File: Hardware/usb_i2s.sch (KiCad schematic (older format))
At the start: 13 parts, among them J2 USB_B, U8 USBLC6-2SC6, U9 PCM2707, Y1 12 MHz

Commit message: started routing
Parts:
- Y1: symbol Device:Crystal -> Device:Crystal_GND24
- renumbered C2 to C76, C7 to C77, C9 to C78, J2 to J8, R11 to R39, R13 to R40, R18 to R41, R19 to R42, R20 to R43, R37 to R44
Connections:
- wire segments 85 -> 91
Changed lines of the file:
@@
 $Descr A4 11693 8268
 encoding utf-8
-Sheet 7 7
+Sheet 6 8
 Title ""
 Date ""
@@
 $EndComp
 $Comp
-L Device:Crystal Y?
+L Device:Crystal_GND24 Y?
 U 1 1 61ACFD71
 P 2200 4950
@@
 AR Path="/5AFACF29/61ACFD77" Ref="C?"  Part="1"
 AR Path="/61ACFD77" Ref="C?"  Part="1"
-AR Path="/61AABE2E/61ACFD77" Ref="C7"  Part="1"
-F 0 "C7" H 2565 5196 50  0000 L CNN
+AR Path="/61AABE2E/61ACFD77" Ref="C77"  Part="1"
+F 0 "C77" H 2565 5196 50  0000 L CNN
 F 1 "33p" H 2565 5105 50  0000 L CNN
 F 2 "Capacitor_SMD:C_0603_1608Metric_Pad1.08x0.95mm_HandSolder" H 2488 5000 50  0001 C CNN
@@
 $EndComp
 $Comp
-L dsp-amplifier-x4-rescue:GND #PWR?
+L power:GND #PWR?
 U 1 1 61ACFD7D
 P 3550 6050
 AR Path="/61ACFD7D" Ref="#PWR?"  Part="1"
-AR Path="/61AABE2E/61ACFD7D" Ref="#PWR0129"  Part="1"
-F 0 "#PWR0129" H 3550 5800 50  0001 C CNN
+AR Path="/61AABE2E/61ACFD7D" Ref="#PWR0107"  Part="1"
+F 0 "#PWR0107" H 3550 5800 50  0001 C CNN
 F 1 "GND" H 3550 5900 50  0000 C CNN
 F 2 "" H 3550 6050 50  0001 C CNN
@@
 AR Path="/5AFACF29/61ACFD91" Ref="C?"  Part="1"
 AR Path="/61ACFD91" Ref="C?"  Part="1"
-AR Path="/61AABE2E/61ACFD91" Ref="C2"  Part="1"
-F 0 "C2" H 2065 5196 50  0000 L CNN
+AR Path="/61AABE2E/61ACFD91" Ref="C76"  Part="1"
+F 0 "C76" H 2065 5196 50  0000 L CNN
 F 1 "33p" H 2065 5105 50  0000 L CNN
 F 2 "Capacitor_SMD:C_0603_1608Metric_Pad1.08x0.95mm_HandSolder" H 1988 5000 50  0001 C CNN
@@
 	2450 4950 2450 5000
 $Comp
-L dsp-amplifier-x4-rescue:GND #PWR?
+L power:GND #PWR?
 U 1 1 61ACFD9B
 P 2200 5450
 AR Path="/61ACFD9B" Ref="#PWR?"  Part="1"
-AR Path="/61AABE2E/61ACFD9B" Ref="#PWR0130"  Part="1"
-F 0 "#PWR0130" H 2200 5200 50  0001 C CNN
+AR Path="/61AABE2E/61ACFD9B" Ref="#PWR0104"  Part="1"
+F 0 "#PWR0104" H 2200 5200 50  0001 C CNN
 F 1 "GND" H 2200 5300 50  0000 C CNN
 F 2 "" H 2200 5450 50  0001 C CNN
@@
 P 4150 3200
 AR Path="/61ACFDAE" Ref="#PWR?"  Part="1"
-AR Path="/61AABE2E/61ACFDAE" Ref="#PWR0131"  Part="1"
-F 0 "#PWR0131" H 4150 3050 50  0001 C CNN
+AR Path="/61AABE2E/61ACFDAE" Ref="#PWR0110"  Part="1"
+F 0 "#PWR0110" H 4150 3050 50  0001 C CNN
 F 1 "+3.3V" H 4165 3373 50  0000 C CNN
 F 2 "" H 4150 3200 50  0001 C CNN
@@
 P 3650 3200
 AR Path="/61ACFDC0" Ref="#PWR?"  Part="1"
-AR Path="/61AABE2E/61ACFDC0" Ref="#PWR0132"  Part="1"
-F 0 "#PWR0132" H 3650 3050 50  0001 C CNN
+AR Path="/61AABE2E/61ACFDC0" Ref="#PWR0109"  Part="1"
+F 0 "#PWR0109" H 3650 3050 50  0001 C CNN
 F 1 "VBUS" H 3665 3373 50  0000 C CNN
 F 2 "" H 3650 3200 50  0001 C CNN
@@
 AR Path="/5AFACF29/61ACFDC6" Ref="C?"  Part="1"
 AR Path="/61ACFDC6" Ref="C?"  Part="1"
-AR Path="/61AABE2E/61ACFDC6" Ref="C9"  Part="1"
-F 0 "C9" H 4565 5446 50  0000 L CNN
+AR Path="/61AABE2E/61ACFDC6" Ref="C78"  Part="1"
+F 0 "C78" H 4565 5446 50  0000 L CNN
 F 1 "100n" H 4565 5355 50  0000 L CNN
 F 2 "Capacitor_SMD:C_0603_1608Metric_Pad1.08x0.95mm_HandSolder" H 4488 5250 50  0001 C CNN
@@
 P 3350 3200
 AR Path="/61ACFDD5" Ref="#PWR?"  Part="1"
-AR Path="/61AABE2E/61ACFDD5" Ref="#PWR0142"  Part="1"
-F 0 "#PWR0142" H 3350 3050 50  0001 C CNN
+AR Path="/61AABE2E/61ACFDD5" Ref="#PWR0106"  Part="1"
+F 0 "#PWR0106" H 3350 3050 50  0001 C CNN
 F 1 "+3.3V" H 3365 3373 50  0000 C CNN
 F 2 "" H 3350 3200 50  0001 C CNN
@@
 P 1950 3400
 AR Path="/61ACFDE5" Ref="#PWR?"  Part="1"
-AR Path="/61AABE2E/61ACFDE5" Ref="#PWR0143"  Part="1"
-F 0 "#PWR0143" H 1950 3250 50  0001 C CNN
+AR Path="/61AABE2E/61ACFDE5" Ref="#PWR0101"  Part="1"
+F 0 "#PWR0101" H 1950 3250 50  0001 C CNN
 F 1 "+3.3V" H 1965 3573 50  0000 C CNN
 F 2 "" H 1950 3400 50  0001 C CNN
@@
 $EndComp
 $Comp
-L dsp-amplifier-x4-rescue:GND #PWR?
+L power:GND #PWR?
 U 1 1 61ACFDEB
 P 1950 3650
 AR Path="/61ACFDEB" Ref="#PWR?"  Part="1"
-AR Path="/61AABE2E/61ACFDEB" Ref="#PWR0144"  Part="1"
-F 0 "#PWR0144" H 1950 3400 50  0001 C CNN
+AR Path="/61AABE2E/61ACFDEB" Ref="#PWR0102"  Part="1"
+F 0 "#PWR0102" H 1950 3400 50  0001 C CNN
 F 1 "GND" H 1950 3500 50  0000 C CNN
 F 2 "" H 1950 3650 50  0001 C CNN
@@
 PSEL
 $Comp
-L dsp-amplifier-x4-rescue:GND #PWR?
+L power:GND #PWR?
 U 1 1 61ACFDF8
 P 1950 4050
 AR Path="/61ACFDF8" Ref="#PWR?"  Part="1"
-AR Path="/61AABE2E/61ACFDF8" Ref="#PWR0145"  Part="1"
-F 0 "#PWR0145" H 1950 3800 50  0001 C CNN
+AR Path="/61AABE2E/61ACFDF8" Ref="#PWR0103"  Part="1"
+F 0 "#PWR0103" H 1950 3800 50  0001 C CNN
 F 1 "GND" H 1950 3900 50  0000 C CNN
 F 2 "" H 1950 4050 50  0001 C CNN
@@
 P 4550 3850
 AR Path="/61ACFE10" Ref="R?"  Part="1"
-AR Path="/61AABE2E/61ACFE10" Ref="R18"  Part="1"
-F 0 "R18" V 4343 3850 50  0000 C CNN
+AR Path="/61AABE2E/61ACFE10" Ref="R41"  Part="1"
+F 0 "R41" V 4343 3850 50  0000 C CNN
 F 1 "33" V 4434 3850 50  0000 C CNN
 F 2 "Resistor_SMD:R_0603_1608Metric_Pad0.98x0.95mm_HandSolder" V 4480 3850 50  0001 C CNN
@@
 P 4550 3950
 AR Path="/61ACFE16" Ref="R?"  Part="1"
-AR Path="/61AABE2E/61ACFE16" Ref="R19"  Part="1"
-F 0 "R19" V 4343 3950 50  0001 C CNN
+AR Path="/61AABE2E/61ACFE16" Ref="R42"  Part="1"
+F 0 "R42" V 4343 3950 50  0001 C CNN
 F 1 "33" V 4434 3950 50  0001 C CNN
 F 2 "Resistor_SMD:R_0603_1608Metric_Pad0.98x0.95mm_HandSolder" V 4480 3950 50  0001 C CNN
@@
 P 4550 4050
 AR Path="/61ACFE1C" Ref="R?"  Part="1"
-AR Path="/61AABE2E/61ACFE1C" Ref="R20"  Part="1"
-F 0 "R20" V 4343 4050 50  0001 C CNN
+AR Path="/61AABE2E/61ACFE1C" Ref="R43"  Part="1"
+F 0 "R43" V 4343 4050 50  0001 C CNN
 F 1 "33" V 4434 4050 50  0001 C CNN
 F 2 "Resistor_SMD:R_0603_1608Metric_Pad0.98x0.95mm_HandSolder" V 4480 4050 50  0001 C CNN
@@
 	4400 3850 4350 3850
 $Comp
-L power:VBUS #PWR0163
+L power:VBUS #PWR0100
 U 1 1 61AEB454
 P 1850 1250
-F 0 "#PWR0163" H 1850 1100 50  0001 C CNN
+F 0 "#PWR0100" H 1850 1100 50  0001 C CNN
 F 1 "VBUS" H 1865 1423 50  0000 C CNN
 F 2 "" H 1850 1250 50  0001 C CNN
@@
 	1850 1350 1850 1250
 $Comp
-L dsp-amplifier-x4-rescue:GND #PWR0164
+L power:GND #PWR098
 U 1 1 61AEB45C
 P 1250 2050
-F 0 "#PWR0164" H 1250 1800 50  0001 C CNN
+F 0 "#PWR098" H 1250 1800 50  0001 C CNN
 F 1 "GND" H 1250 1900 50  0000 C CNN
 F 2 "" H 1250 2050 50  0001 C CNN
@@
 	3300 2050 3950 2050
 $Comp
-L power:VBUS #PWR0165
+L power:VBUS #PWR0108
 U 1 1 61AEB470
 P 3650 1500
-F 0 "#PWR0165" H 3650 1350 50  0001 C CNN
+F 0 "#PWR0108" H 3650 1350 50  0001 C CNN
 F 1 "VBUS" H 3665 1673 50  0000 C CNN
 F 2 "" H 3650 1500 50  0001 C CNN
@@
 	3650 1600 3600 1600
 $Comp
-L dsp-amplifier-x4-rescue:GND #PWR0166
+L power:GND #PWR0105
 U 1 1 61AEB478
 P 2750 1700
-F 0 "#PWR0166" H 2750 1450 50  0001 C CNN
+F 0 "#PWR0105" H 2750 1450 50  0001 C CNN
 F 1 "GND" H 2750 1550 50  0000 C CNN
 F 2 "" H 2750 1700 50  0001 C CNN
@@
 Wire Wire Line
 	2750 1600 2750 1700
-Wire Wire Line
-	1650 1550 2600 1550
-Wire Wire Line
-	1650 1650 2600 1650
-Text Label 4350 2050 0    60   ~ 0
+Text Label 4750 1150 2    60   ~ 0
 USB-DM
-Text Label 4350 1150 0    60   ~ 0
+Text Label 4750 2050 2    60   ~ 0
 USB-DP
 $Comp
-L Device:R R11
+L Device:R R39
 U 1 1 61AEB484
 P 4100 1150
-F 0 "R11" V 3893 1150 50  0000 C CNN
+F 0 "R39" V 3893 1150 50  0000 C CNN
 F 1 "33" V 3984 1150 50  0000 C CNN
 F 2 "Resistor_SMD:R_0603_1608Metric_Pad0.98x0.95mm_HandSolder" V 4030 1150 50  0001 C CNN
@@
 $EndComp
 $Comp
-L Device:R R13
+L Device:R R40
 U 1 1 61AEB48A
 P 4100 2050
-F 0 "R13" V 3893 2050 50  0000 C CNN
+F 0 "R40" V 3893 2050 50  0000 C CNN
 F 1 "33" V 3984 2050 50  0000 C CNN
 F 2 "Resistor_SMD:R_0603_1608Metric_Pad0.98x0.95mm_HandSolder" V 4030 2050 50  0001 C CNN
@@
 	4750 1150 4250 1150
 $Comp
-L Connector:USB_B J2
+L Connector:USB_B J8
 U 1 1 61AEB492
 P 1350 1550
-F 0 "J2" H 1407 2017 50  0000 C CNN
+F 0 "J8" H 1407 2017 50  0000 C CNN
 F 1 "USB_B" H 1407 1926 50  0000 C CNN
 F 2 "Connector_USB:USB_B_TE_5787834_Vertical" H 1500 1500 50  0001 C CNN
@@
 P 4550 4350
 AR Path="/61B18C42" Ref="R?"  Part="1"
-AR Path="/61AABE2E/61B18C42" Ref="R37"  Part="1"
-F 0 "R37" V 4343 4350 50  0001 C CNN
+AR Path="/61AABE2E/61B18C42" Ref="R44"  Part="1"
+F 0 "R44" V 4343 4350 50  0001 C CNN
 F 1 "33" V 4434 4350 50  0001 C CNN
 F 2 "Resistor_SMD:R_0603_1608Metric_Pad0.98x0.95mm_HandSolder" V 4480 4350 50  0001 C CNN
@@
 Wire Wire Line
 	4750 4350 4700 4350
+Wire Wire Line
+	2200 5150 2200 5400
+$Comp
+L power:GND #PWR?
+U 1 1 609F2BC8
+P 1750 5450
+AR Path="/609F2BC8" Ref="#PWR?"  Part="1"
+AR Path="/61AABE2E/609F2BC8" Ref="#PWR099"  Part="1"
+F 0 "#PWR099" H 1750 5200 50  0001 C CNN
+F 1 "GND" H 1750 5300 50  0000 C CNN
+F 2 "" H 1750 5450 50  0001 C CNN
+F 3 "" H 1750 5450 50  0001 C CNN
+	1    1750 5450
+	1    0    0    -1
+$EndComp
+Wire Wire Line
+	1750 5450 1750 4550
+Wire Wire Line
+	1750 4550 2200 4550
+Wire Wire Line
+	2200 4550 2200 4750
+Wire Wire Line
+	2500 1650 1650 1650
+Wire Wire Line
+	2500 1550 1650 1550
+Wire Wire Line
+	2600 1550 2500 1650
+Wire Wire Line
+	2500 1550 2600 1650
 $EndSCHEMATC

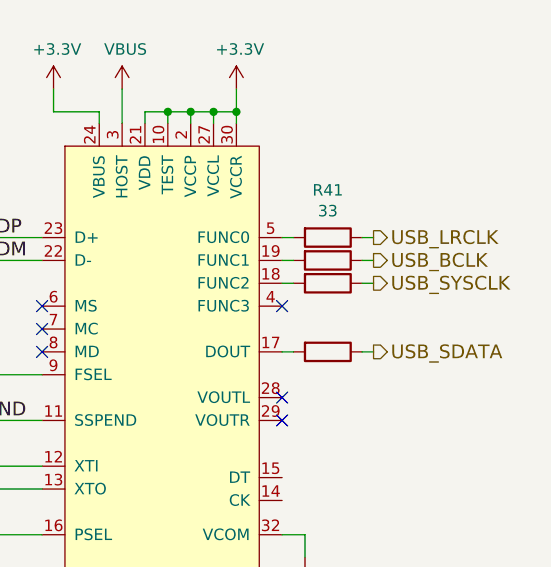
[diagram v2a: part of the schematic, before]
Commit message: routing, added 4 layers
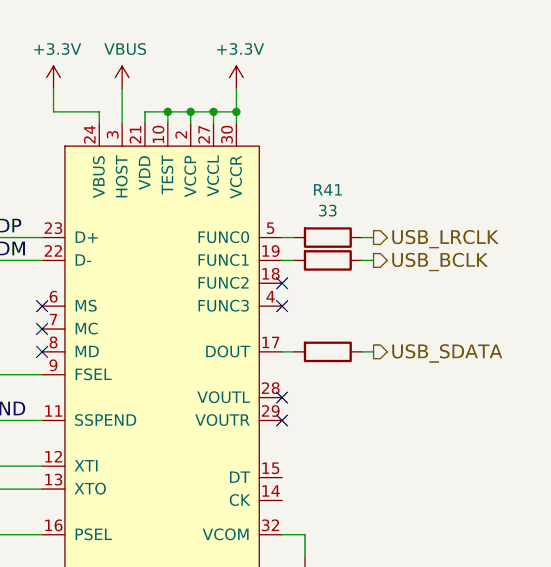
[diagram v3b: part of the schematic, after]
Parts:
- removed R43: 33, Resistor_SMD:R_0603_1608Metric_Pad0.98x0.95mm_HandSolder, symbol Device:R
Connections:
- net labels removed: USB_SYSCLK
- wire segments 91 -> 89
- no-connect marks 6 -> 7
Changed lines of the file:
@@
 Wire Wire Line
 	1950 4000 2350 4000
-NoConn ~ 4350 4150
 NoConn ~ 3300 4150
 NoConn ~ 3300 4250
@@
 	0    1    1    0
 $EndComp
-$Comp
-L Device:R R?
-U 1 1 61ACFE1C
-P 4550 4050
-AR Path="/61ACFE1C" Ref="R?"  Part="1"
-AR Path="/61AABE2E/61ACFE1C" Ref="R43"  Part="1"
-F 0 "R43" V 4343 4050 50  0001 C CNN
-F 1 "33" V 4434 4050 50  0001 C CNN
-F 2 "Resistor_SMD:R_0603_1608Metric_Pad0.98x0.95mm_HandSolder" V 4480 4050 50  0001 C CNN
-F 3 "~" H 4550 4050 50  0001 C CNN
-	1    4550 4050
-	0    1    1    0
-$EndComp
-Wire Wire Line
-	4400 4050 4350 4050
 Wire Wire Line
 	4350 3950 4400 3950
@@
 Wire Wire Line
 	4700 3950 4750 3950
-Wire Wire Line
-	4750 4050 4700 4050
 Text HLabel 4750 4350 2    60   Output ~ 0
 USB_SDATA
@@
 Wire Wire Line
 	2500 1550 2600 1650
-Text HLabel 4750 4050 2    60   Output ~ 0
-USB_SYSCLK
+NoConn ~ 4350 4050
+NoConn ~ 4350 4150
 $EndSCHEMATC

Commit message: bugfixes, made smaller
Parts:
- removed C78: 100n, Capacitor_SMD:C_0603_1608Metric_Pad1.08x0.95mm_HandSolder, symbol Device:C
- added C83, C84, C85: 10u, Capacitor_SMD:C_1206_3216Metric_Pad1.33x1.80mm_HandSolder, symbol Device:C
- added C86, C87: 100n, Capacitor_SMD:C_0603_1608Metric_Pad1.08x0.95mm_HandSolder, symbol Device:C
- added C88, C89: 1u, Capacitor_SMD:C_0805_2012Metric_Pad1.18x1.45mm_HandSolder, symbol Device:C
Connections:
- wire segments 89 -> 113
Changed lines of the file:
@@
-	1    0    0    -1
-$EndComp
-$Comp
-L Device:C C?
-U 1 1 61ACFDC6
-P 4450 5400
-AR Path="/5AFACF29/61ACFDC6" Ref="C?"  Part="1"
-AR Path="/61ACFDC6" Ref="C?"  Part="1"
-AR Path="/61AABE2E/61ACFDC6" Ref="C78"  Part="1"
-F 0 "C78" H 4565 5446 50  0000 L CNN
-F 1 "100n" H 4565 5355 50  0000 L CNN
-F 2 "Capacitor_SMD:C_0603_1608Metric_Pad1.08x0.95mm_HandSolder" H 4488 5250 50  0001 C CNN
-F 3 "~" H 4450 5400 50  0001 C CNN
-	1    4450 5400
 	1    0    0    -1
 $EndComp
@@
 Wire Wire Line
 	2500 1550 2600 1650
+NoConn ~ 4350 4150
+$Comp
+L Device:C C?
+U 1 1 60A7FB68
+P 6850 4000
+AR Path="/5AF9FF80/60A7FB68" Ref="C?"  Part="1"
+AR Path="/60A7FB68" Ref="C?"  Part="1"
+AR Path="/61AABE2E/60A7FB68" Ref="C86"  Part="1"
+F 0 "C86" H 6900 4100 50  0000 L CNN
+F 1 "100n" H 6900 3900 50  0000 L CNN
+F 2 "Capacitor_SMD:C_0603_1608Metric_Pad1.08x0.95mm_HandSolder" V 6550 4140 50  0001 C CNN
+F 3 "~" V 6550 4140 50  0001 C CNN
+F 4 "GRM31CR71H475KA12L" H 6850 4000 60  0001 C CNN "Mfr.Nr."
+	1    6850 4000
+	1    0    0    -1
+$EndComp
+Wire Wire Line
+	6850 3750 6850 3850
+Connection ~ 6500 3750
+Wire Wire Line
+	6500 3750 6850 3750
+$Comp
+L power:GND #PWR?
+U 1 1 60A7FB72
+P 6500 4250
+AR Path="/60A7FB72" Ref="#PWR?"  Part="1"
+AR Path="/61AABE2E/60A7FB72" Ref="#PWR0120"  Part="1"
+F 0 "#PWR0120" H 6500 4000 50  0001 C CNN
+F 1 "GND" H 6500 4100 50  0000 C CNN
+F 2 "" H 6500 4250 50  0001 C CNN
+F 3 "" H 6500 4250 50  0001 C CNN
+	1    6500 4250
+	1    0    0    -1
+$EndComp
+Wire Wire Line
+	6500 3450 6500 3750
+Wire Wire Line
+	6500 4200 6850 4200
+Wire Wire Line
+	6850 4200 6850 4150
+Connection ~ 6500 4200
+Wire Wire Line
+	6500 4200 6500 4250
+$Comp
+L power:+3.3V #PWR?
+U 1 1 60A82673
+P 6500 3450
+AR Path="/60A82673" Ref="#PWR?"  Part="1"
+AR Path="/61AABE2E/60A82673" Ref="#PWR0121"  Part="1"
+F 0 "#PWR0121" H 6500 3300 50  0001 C CNN
+F 1 "+3.3V" H 6515 3623 50  0000 C CNN
+F 2 "" H 6500 3450 50  0001 C CNN
+F 3 "" H 6500 3450 50  0001 C CNN
+	1    6500 3450
+	1    0    0    -1
+$EndComp
+$Comp
+L Device:C C?
+U 1 1 60A879BB
+P 6150 4000
+AR Path="/5AF9FF80/60A879BB" Ref="C?"  Part="1"
+AR Path="/60A879BB" Ref="C?"  Part="1"
+AR Path="/61AABE2E/60A879BB" Ref="C84"  Part="1"
+F 0 "C84" H 6200 4100 50  0000 L CNN
+F 1 "10u" H 6200 3900 50  0000 L CNN
+F 2 "Capacitor_SMD:C_1206_3216Metric_Pad1.33x1.80mm_HandSolder" V 5850 4140 50  0001 C CNN
+F 3 "http://www.murata.com/products/catalog/pdf/c02e.pdf" V 5850 4140 50  0001 C CNN
+F 4 "GRM31CR71H475KA12L" H 6150 4000 60  0001 C CNN "Mfr.Nr."
+	1    6150 4000
+	1    0    0    -1
+$EndComp
+$Comp
+L Device:C C?
+U 1 1 60A8AF5C
+P 4450 5400
+AR Path="/5AF9FF80/60A8AF5C" Ref="C?"  Part="1"
+AR Path="/60A8AF5C" Ref="C?"  Part="1"
+AR Path="/61AABE2E/60A8AF5C" Ref="C83"  Part="1"
+F 0 "C83" H 4500 5500 50  0000 L CNN
+F 1 "10u" H 4500 5300 50  0000 L CNN
+F 2 "Capacitor_SMD:C_1206_3216Metric_Pad1.33x1.80mm_HandSolder" V 4150 5540 50  0001 C CNN
+F 3 "http://www.murata.com/products/catalog/pdf/c02e.pdf" V 4150 5540 50  0001 C CNN
+F 4 "GRM31CR71H475KA12L" H 4450 5400 60  0001 C CNN "Mfr.Nr."
+	1    4450 5400
+	1    0    0    -1
+$EndComp
+$Comp
+L Device:C C?
+U 1 1 60A95304
+P 7650 4000
+AR Path="/5AFACF29/60A95304" Ref="C?"  Part="1"
+AR Path="/5AFACF57/60A95304" Ref="C?"  Part="1"
+AR Path="/61AABE2E/60A95304" Ref="C88"  Part="1"
+F 0 "C88" H 7765 4046 50  0000 L CNN
+F 1 "1u" H 7765 3955 50  0000 L CNN
+F 2 "Capacitor_SMD:C_0805_2012Metric_Pad1.18x1.45mm_HandSolder" H 7688 3850 50  0001 C CNN
+F 3 "~" H 7650 4000 50  0001 C CNN
+	1    7650 4000
+	1    0    0    -1
+$EndComp
+$Comp
+L Device:C C?
+U 1 1 60A97BBA
+P 8100 4000
+AR Path="/5AFACF29/60A97BBA" Ref="C?"  Part="1"
+AR Path="/5AFACF57/60A97BBA" Ref="C?"  Part="1"
+AR Path="/61AABE2E/60A97BBA" Ref="C89"  Part="1"
+F 0 "C89" H 8215 4046 50  0000 L CNN
+F 1 "1u" H 8215 3955 50  0000 L CNN
+F 2 "Capacitor_SMD:C_0805_2012Metric_Pad1.18x1.45mm_HandSolder" H 8138 3850 50  0001 C CNN
+F 3 "~" H 8100 4000 50  0001 C CNN
+	1    8100 4000
+	1    0    0    -1
+$EndComp
+Wire Wire Line
+	8100 3850 8100 3750
+Wire Wire Line
+	8100 3750 7650 3750
+Wire Wire Line
+	7650 3850 7650 3750
+Connection ~ 7650 3750
+Wire Wire Line
+	7650 3750 7250 3750
+Wire Wire Line
+	7250 4200 7650 4200
+Wire Wire Line
+	7650 4200 7650 4150
+Wire Wire Line
+	7650 4200 8100 4200
+Wire Wire Line
+	8100 4200 8100 4150
+Connection ~ 7650 4200
+Wire Wire Line
+	6150 3850 6150 3750
+Wire Wire Line
+	6150 3750 6500 3750
+Wire Wire Line
+	6150 4150 6150 4200
+Wire Wire Line
+	6150 4200 6500 4200
+$Comp
+L Device:C C?
+U 1 1 60AB311A
+P 6500 4000
+AR Path="/5AF9FF80/60AB311A" Ref="C?"  Part="1"
+AR Path="/60AB311A" Ref="C?"  Part="1"
+AR Path="/61AABE2E/60AB311A" Ref="C85"  Part="1"
+F 0 "C85" H 6550 4100 50  0000 L CNN
+F 1 "10u" H 6550 3900 50  0000 L CNN
+F 2 "Capacitor_SMD:C_1206_3216Metric_Pad1.33x1.80mm_HandSolder" V 6200 4140 50  0001 C CNN
+F 3 "http://www.murata.com/products/catalog/pdf/c02e.pdf" V 6200 4140 50  0001 C CNN
+F 4 "GRM31CR71H475KA12L" H 6500 4000 60  0001 C CNN "Mfr.Nr."
+	1    6500 4000
+	1    0    0    -1
+$EndComp
+$Comp
+L Device:C C?
+U 1 1 60AB6D9C
+P 7250 4000
+AR Path="/5AF9FF80/60AB6D9C" Ref="C?"  Part="1"
+AR Path="/60AB6D9C" Ref="C?"  Part="1"
+AR Path="/61AABE2E/60AB6D9C" Ref="C87"  Part="1"
+F 0 "C87" H 7300 4100 50  0000 L CNN
+F 1 "100n" H 7300 3900 50  0000 L CNN
+F 2 "Capacitor_SMD:C_0603_1608Metric_Pad1.08x0.95mm_HandSolder" V 6950 4140 50  0001 C CNN
+F 3 "~" V 6950 4140 50  0001 C CNN
+F 4 "GRM31CR71H475KA12L" H 7250 4000 60  0001 C CNN "Mfr.Nr."
+	1    7250 4000
+	1    0    0    -1
+$EndComp
+Wire Wire Line
+	7250 4150 7250 4200
+Wire Wire Line
+	7250 3850 7250 3750
+Wire Wire Line
+	6850 3750 7250 3750
+Connection ~ 6850 3750
+Connection ~ 7250 3750
+Wire Wire Line
+	7250 4200 6850 4200
+Connection ~ 7250 4200
+Connection ~ 6850 4200
+Wire Wire Line
+	6500 4150 6500 4200
+Wire Wire Line
+	6500 3850 6500 3750
 NoConn ~ 4350 4050
-NoConn ~ 4350 4150
 $EndSCHEMATC

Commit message: hardware bugfixes
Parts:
- added R33: 1M, Resistor_SMD:R_0603_1608Metric_Pad0.98x0.95mm_HandSolder, symbol Device:R
- added R34, R40: 1.5k, Resistor_SMD:R_0603_1608Metric_Pad0.98x0.95mm_HandSolder, symbol Device:R
- renumbered C83 to C78, C84 to C79, C85 to C80, C86 to C81, C87 to C82, C88 to C83, C89 to C84, R39 to R35, R40 to R36, R41 to R37, R42 to R38, R44 to R39, U9 to U10, U8 to U9
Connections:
- net labels added: USB_SUSPEND
- net labels removed: SSPEND
- wire segments 113 -> 121
- no-connect marks 7 -> 8

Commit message: various bugfixes
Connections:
- net +3V3: no longer R34.2
- net VBUS: now also R34.2
- net at C76.1, U10.12 (XTI), Y1.1: now also R33.2; no longer R33.1
- net at C77.1, U10.13 (XTO), Y1.3: now also R33.1; no longer R33.2
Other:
- moved on the sheet: C76, C77, C79, C80, C81, C82, C83, C84, R33, Y1
